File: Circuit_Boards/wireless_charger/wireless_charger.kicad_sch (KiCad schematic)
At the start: 117 parts

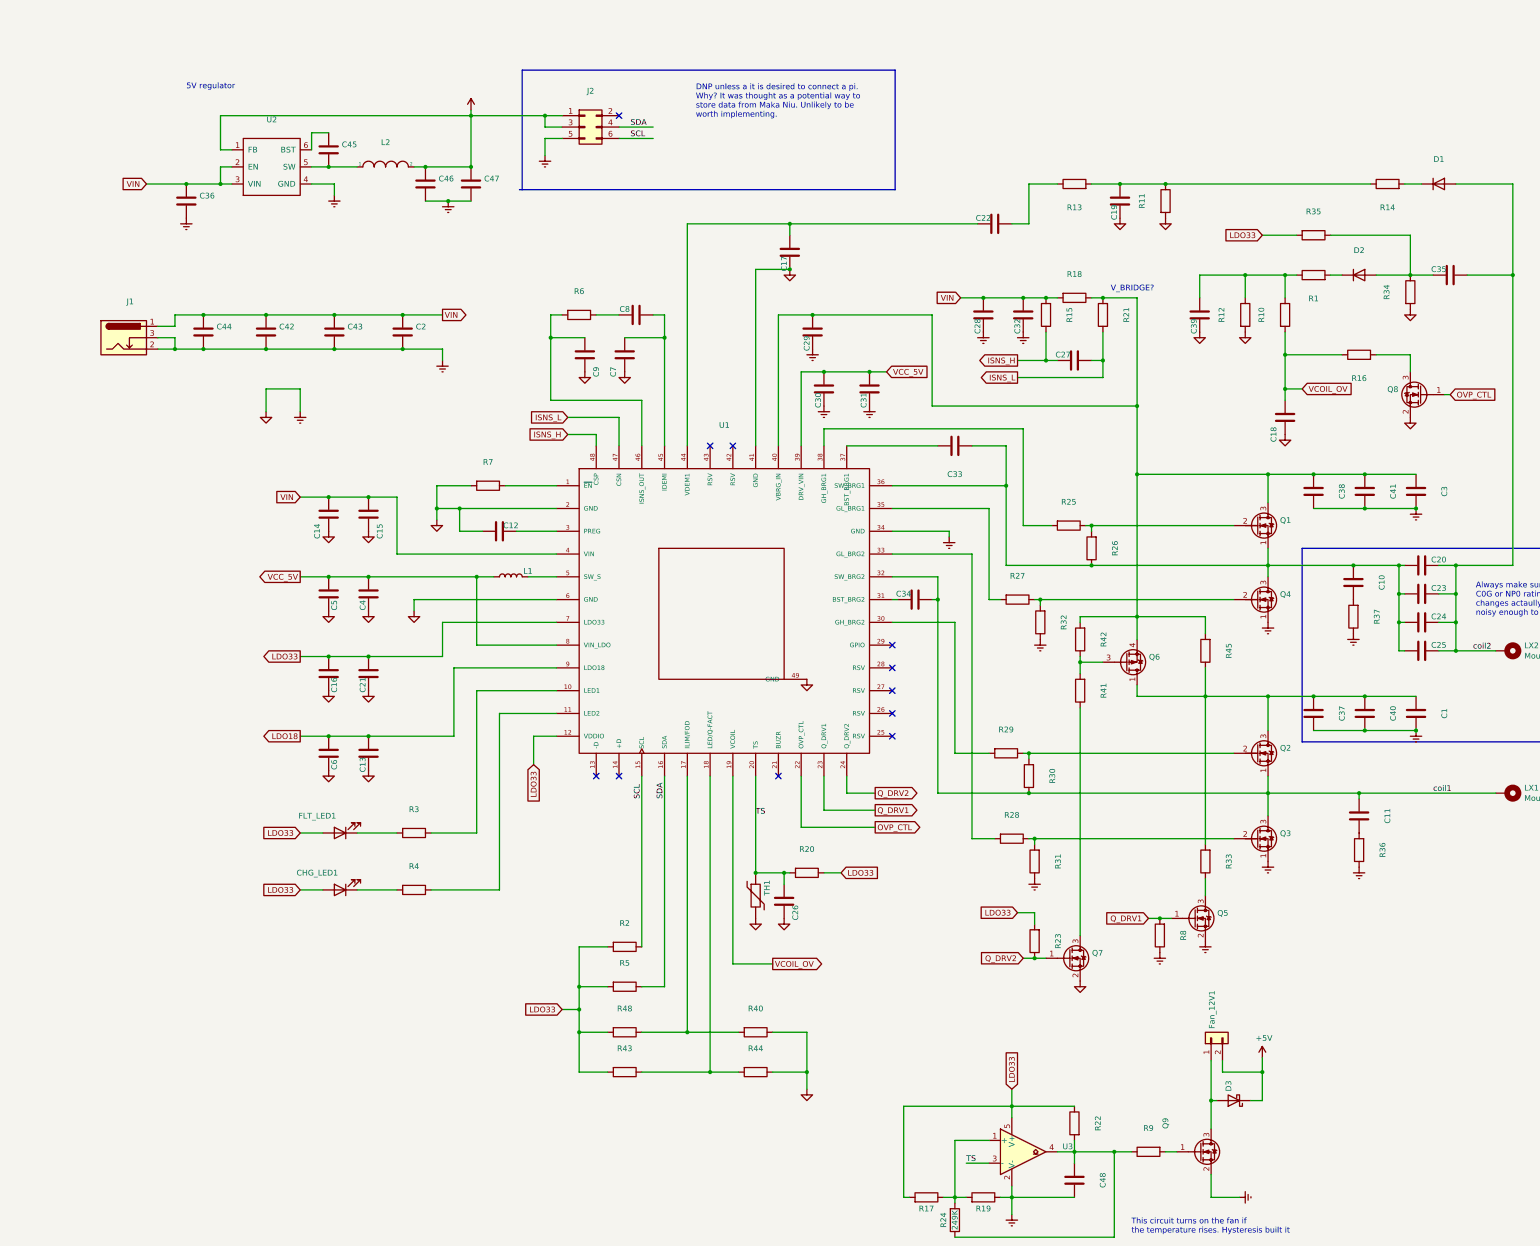
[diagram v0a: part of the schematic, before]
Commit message: cleaned up a bit and mainly added the LED board to the repo
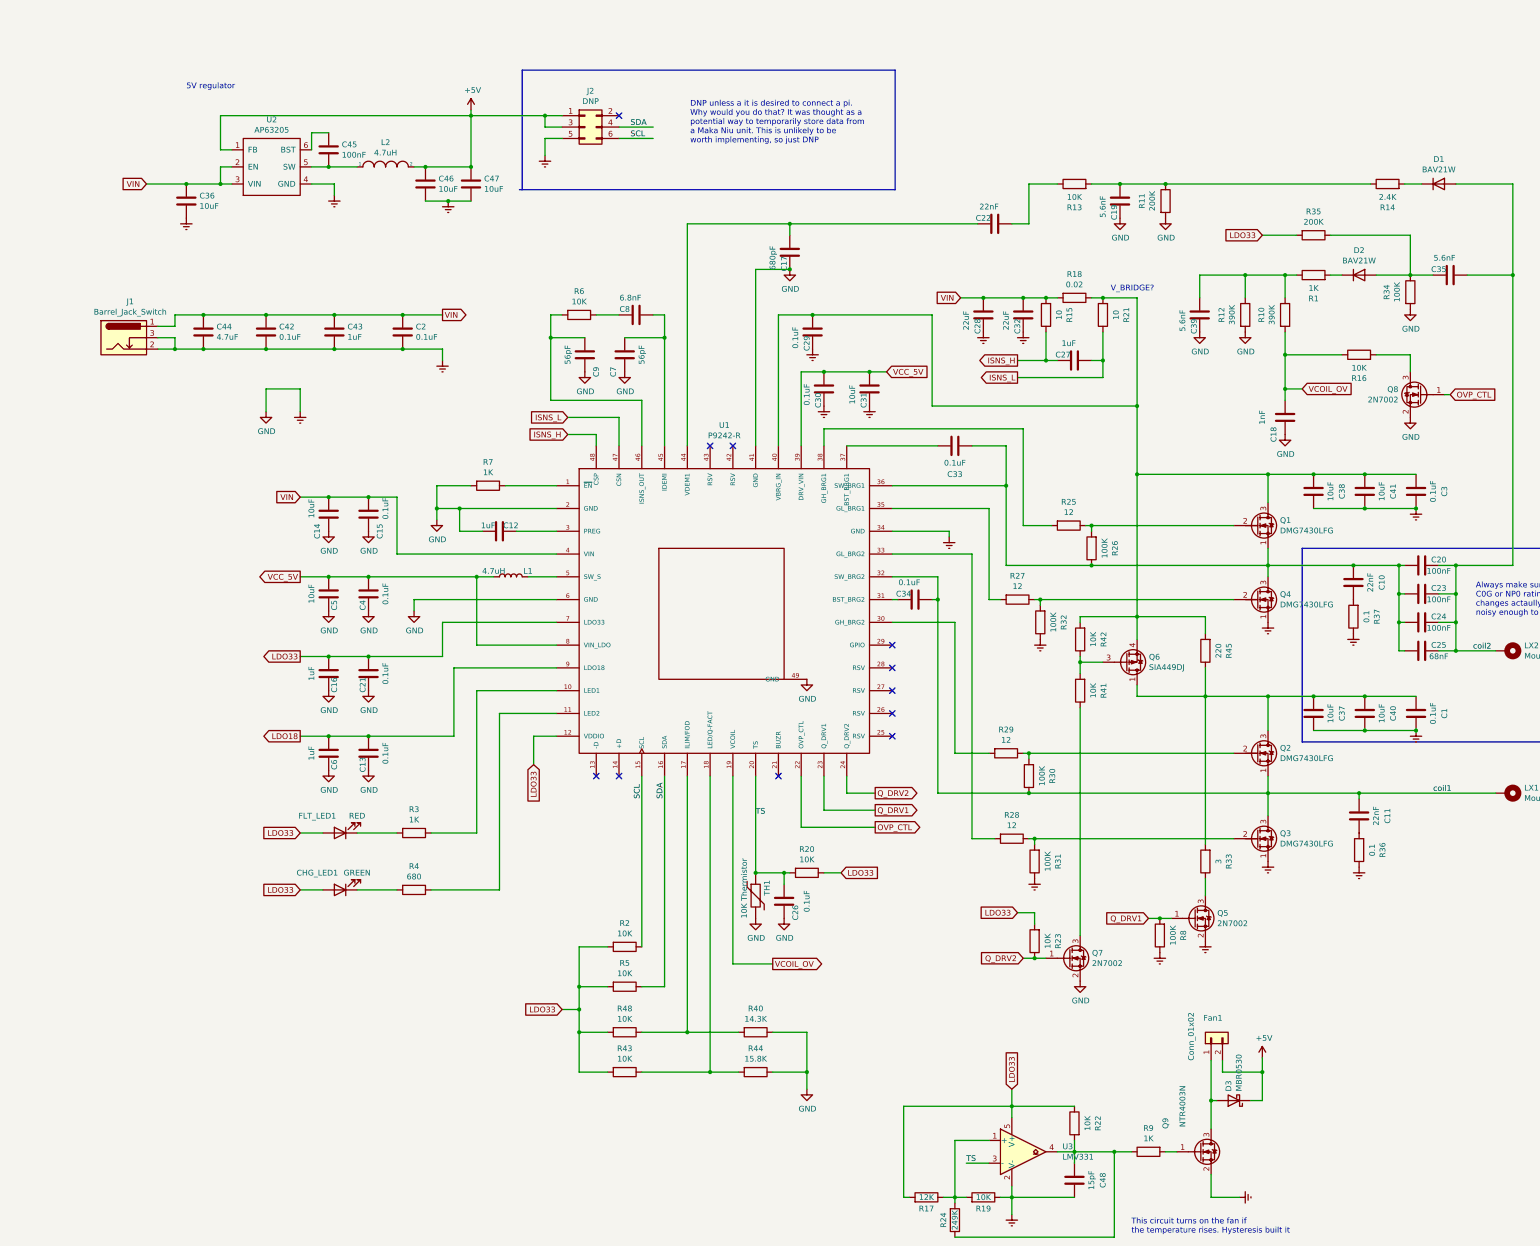
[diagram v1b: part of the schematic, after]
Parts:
- C1, C13, C15, C2, C21, C26, C29, C3, C30, C33, C34, C4: value (none) -> 0.1uF; footprint (none) -> Capacitor_SMD:C_0402_1005Metric
- C10, C11: value (none) -> 22nF; footprint (none) -> Capacitor_SMD:C_0603_1608Metric
- C12, C16, C27, C6: value (none) -> 1uF; footprint (none) -> Capacitor_SMD:C_0402_1005Metric
- C14, C31, C36, C37, C38, C40, C41, C46, C47, C5: value (none) -> 10uF; footprint (none) -> Capacitor_SMD:C_0603_1608Metric
- C17: value (none) -> 680pF; footprint (none) -> Capacitor_SMD:C_0402_1005Metric
- C18: value (none) -> 1nF; footprint (none) -> Capacitor_SMD:C_0603_1608Metric
- C19, C35, C39: value (none) -> 5.6nF; footprint (none) -> Capacitor_SMD:C_0603_1608Metric
- C20, C23, C24: value (none) -> 100nF; footprint (none) -> Capacitor_SMD:C_1206_3216Metric
- C22: value (none) -> 22nF; footprint (none) -> Capacitor_SMD:C_0402_1005Metric
- C25: value (none) -> 68nF; footprint (none) -> Capacitor_SMD:C_1206_3216Metric
- C28, C32: value (none) -> 22uF; footprint (none) -> Capacitor_SMD:C_1206_3216Metric
- C42: value (none) -> 0.1uF; footprint (none) -> Capacitor_SMD:C_0603_1608Metric
- C43: value (none) -> 1uF; footprint (none) -> Capacitor_SMD:C_0603_1608Metric
- C44: value (none) -> 4.7uF; footprint (none) -> Capacitor_SMD:C_0603_1608Metric
- C45: value (none) -> 100nF; footprint (none) -> Capacitor_SMD:C_0603_1608Metric
- C48: value (none) -> 15pF; footprint (none) -> Capacitor_SMD:C_0402_1005Metric
- C7, C9: value (none) -> 56pF; footprint (none) -> Capacitor_SMD:C_0402_1005Metric
- C8: value (none) -> 6.8nF; footprint (none) -> Capacitor_SMD:C_0402_1005Metric
- CHG_LED1: value (none) -> GREEN; footprint (none) -> LED_SMD:LED_0603_1608Metric
- D1, D2: value (none) -> BAV21W; footprint (none) -> Diode_SMD:D_SOD-123
- D3: value (none) -> MBR0530; footprint (none) -> Diode_SMD:D_SOD-123
- FLT_LED1: value (none) -> RED; footprint (none) -> LED_SMD:LED_0603_1608Metric
- Fan1: renamed from Fan_12V1; value (none) -> Conn_01x02; footprint (none) -> Connector_PinHeader_2.54mm:PinHeader_1x02_P2.54mm_Vertical
- J1: value (none) -> Barrel_Jack_Switch; footprint (none) -> Custom:CUI_PJ-002AH
- J2: value (none) -> DNP; footprint (none) -> Connector_PinHeader_2.54mm:PinHeader_2x03_P2.54mm_Vertical
- L1: value (none) -> 4.7uH; footprint (none) -> Inductor_SMD:L_0603_1608Metric
- L2: value (none) -> 4.7uH; footprint (none) -> Inductor_SMD:L_1008_2520Metric
- Q1, Q2, Q3, Q4: value (none) -> DMG7430LFG; footprint (none) -> Custom:TRANS_DMP3017SFGQ-7_b
- Q5, Q7, Q8: value (none) -> 2N7002; footprint (none) -> Package_TO_SOT_SMD:SOT-23
- Q6: value (none) -> SIA449DJ; footprint (none) -> Package_TO_SOT_SMD:Vishay_PowerPAK_SC70-6L_Single
- Q9: value (none) -> NTR4003N; footprint (none) -> Package_TO_SOT_SMD:SOT-23
- R1, R3, R7, R9: value (none) -> 1K; footprint (none) -> Resistor_SMD:R_0402_1005Metric
- R10, R12: value (none) -> 390K; footprint (none) -> Resistor_SMD:R_0603_1608Metric
- R11, R35: value (none) -> 200K; footprint (none) -> Resistor_SMD:R_0603_1608Metric
- R13, R16, R19, R2, R20, R22, R23, R41, R42, R43, R48, R5, R6: value (none) -> 10K; footprint (none) -> Resistor_SMD:R_0402_1005Metric
- R14: value (none) -> 2.4K; footprint (none) -> Resistor_SMD:R_0402_1005Metric
- R15, R21: value (none) -> 10; footprint (none) -> Resistor_SMD:R_0402_1005Metric
- R17: value (none) -> 12K; footprint (none) -> Resistor_SMD:R_0402_1005Metric
- R18: value (none) -> 0.02; footprint (none) -> Resistor_SMD:R_0805_2012Metric
- R24: footprint (none) -> Resistor_SMD:R_0402_1005Metric
- R25, R27, R28, R29: value (none) -> 12; footprint (none) -> Resistor_SMD:R_0402_1005Metric
- R26, R30, R31, R32, R8: value (none) -> 100K; footprint (none) -> Resistor_SMD:R_0402_1005Metric
- R33: value (none) -> 3; footprint (none) -> Resistor_SMD:R_0805_2012Metric
- R34: value (none) -> 100K; footprint (none) -> Resistor_SMD:R_0603_1608Metric
- R36, R37: value (none) -> 0.1; footprint (none) -> Resistor_SMD:R_0402_1005Metric
- R4: value (none) -> 680; footprint (none) -> Resistor_SMD:R_0402_1005Metric
- R40: value (none) -> 14.3K; footprint (none) -> Resistor_SMD:R_0402_1005Metric
- R44: value (none) -> 15.8K; footprint (none) -> Resistor_SMD:R_0402_1005Metric
- R45: value (none) -> 220; footprint (none) -> Resistor_SMD:R_0805_2012Metric
- TH1: value (none) -> 10K Thermistor; footprint (none) -> Resistor_SMD:R_0805_2012Metric
- U1: value (none) -> P9242-R; footprint (none) -> Custom:QFN40P600X600X100-49N
- U2: value (none) -> AP63205; footprint (none) -> Package_TO_SOT_SMD:TSOT-23-6
- U3: value (none) -> LMV331; footprint (none) -> Package_TO_SOT_SMD:SOT-23-5
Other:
- note added: "DNP unless a it is desired to connect a pi. Why would you do that? It was thought as a potential way to temporarily store data from a Maka Niu unit. This is unlikely to be worth implementing, so just DNP"
- note removed: "DNP unless a it is desired to connect a pi. Why? It was thought as a potential way to store data from Maka Niu. Unlikely to be worth implementing."
